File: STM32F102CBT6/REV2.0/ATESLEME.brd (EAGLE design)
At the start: 35.3 x 57.9 mm, 55 parts, among them U1 ADXL345PATRICK, U3 AMS1117-3.3, U4 STM32F102CBT6, Y2 ABM2B-8.000MHZ-10-1-U-T

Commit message: Revision V2.0.0 was released
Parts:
- removed LPS-1: LPS22, Arduino-Sensors:LPS22H
- removed LPSC1: 4.7uF, SparkFun-Capacitors:0603
- removed LPSC2: 100nF, SparkFun-Capacitors:0603
- added APGLED, MNLED: 4.7k, SparkFun-Resistors:0603-RES
- added IRC, MS5611: 100nF, SparkFun-Capacitors:0603
- added IRR: 100, SparkFun-Resistors:0603-RES
- added IRR1: 1.5k, SparkFun-Resistors:0603-RES
- added LED1: 1k, SparkFun-Resistors:0603-RES
- added LED2: RED, SparkFun-LED:LED-0603
- added RD1, RD2: Blue, SparkFun-LED:LED-0603
- added U2: MS561101BA03-50, MS5611:SON8_MS5611_TEC
- added U5: 38kHz, SparkFun-Sensors:TSOP382
- added X1: JST-XH-04-PIN-LONG-PAD, Rembrandt Electronics - JST XH Connectors v1-0:JST-XH-04-PACKAGE-LONG-PAD
- SCL_3V3, SDA_3V3: value 4.7k -> 10k
- moved RRO 2.44 mm to (7.92, 11.3)
- moved RD 2.42 mm to (7.87, 15.4)
- moved RC3 1.79 mm to (11.8, 12.7)
- moved F 1.35 mm to (10.4, 16.9), turned to 90 degrees
- moved VBAT_U 1.28 mm to (24.5, 23.4)
- moved RC4 1.12 mm to (12.1, 9.35)
- moved S 0.77 mm to (21.5, 49.0)
- moved ESDA 0.68 mm to (32.4, 45.4)
- moved ADXLC 0.68 mm to (7.34, 42.6)
- moved APGRU 0.68 mm to (31.9, 35.7)
- moved ESDM 0.68 mm to (11.3, 50.2)
- moved OSCC1 0.68 mm to (10.4, 35.3)
- moved VDD1 0.68 mm to (25.5, 36.6)
- moved VDD2 0.68 mm to (12.6, 35.8)
- moved BOOT0 0.68 mm to (17.0, 40.8)
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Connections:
- removed net INT1: LPS-1.7, U4.41
- new net IR_OUT: IRR1.1, U4.11, U5.1
- new net LED2: LED1.1, U4.15
- new net N$3: MNLED.1, RD1.A
- new net N$4: APGLED.1, RD2.A
- new net N$5: IRC.1, IRR.1, U5.3
- new net N$6: LED1.2, LED2.A
- new net RX1: U4.31, X1.2
- new net TX1: U4.30, X1.3
- net 3.3V: now also IRR.2, MS5611.1, U2.1, U2.2, X1.1; no longer LPS-1.1, LPS-1.10, LPS-1.6, LPSC1.1, LPSC2.1
- net GND: now also IRC.2, IRR1.2, LED2.C, MS5611.2, RD1.C, RD2.C, U2.3, U2.4, U2.5, U5.2, X1.4; no longer LPS-1.3, LPS-1.5, LPS-1.8, LPS-1.9, LPSC1.2, LPSC2.2
- net SCL_3V3: now also U2.8; no longer LPS-1.2
- net SDA_3V3: now also U2.7; no longer LPS-1.4
- net VAPG: now also APGLED.2
- net VMN: now also MNLED.2
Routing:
- net IR_OUT: track 0.00 -> 20.9 mm, vias 0 -> 1
- net VAPG: track 29.6 -> 49.1 mm
- net TX1: track 0.00 -> 16.6 mm, vias 0 -> 1
- net RX1: track 0.00 -> 14.8 mm, vias 0 -> 1
- net SCL_3V3: track 30.8 -> 19.1 mm
- net INT1: track 10.6 -> 0.00 mm, vias 2 -> 0
- net VMN: track 16.5 -> 22.7 mm
- net N$5: track 0.00 -> 5.12 mm
- net LED2: track 0.00 -> 3.22 mm, vias 0 -> 1
- net N$6: track 0.00 -> 2.39 mm
- net N$3: track 0.00 -> 2.22 mm
- net N$4: track 0.00 -> 2.22 mm
- net VIN: track 113.5 -> 115.7 mm
- net GND: track 1.24 -> 2.89 mm, vias 21 -> 19
- net 3.3V: track 142.0 -> 140.5 mm
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
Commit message: Version 2.0 was updated by brain.dll
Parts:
- added HOLDR, WPR: 10k, SparkFun-Resistors:0603-RES
- added IC1: WS2811-SOP8, adafruit:SO08-SKINNYPADS
- moved IRC 30.2 mm to (33.3, 26.6), flipped to the bottom, turned to 90 degrees
- moved IRR 29.1 mm to (31.0, 26.7), flipped to the bottom
- moved IRR1 28.4 mm to (32.9, 15.8), flipped to the bottom, turned to 270 degrees
- moved S2 28.1 mm to (33.3, 46.5), flipped to the bottom
- moved MNRU 28.0 mm to (33.2, 49.2), flipped to the bottom
- moved U5 27.3 mm to (32.8, 21.4), turned to 90 degrees
- moved MNRD 27.1 mm to (32.8, 40.0), flipped to the bottom
- moved ESDA 26.2 mm to (6.15, 45.9), flipped to the bottom
- moved APGRD 25.4 mm to (6.55, 32.7), flipped to the bottom
- moved APGRU 25.4 mm to (6.58, 36.2), flipped to the bottom
- moved Y2 24.2 mm to (31.3, 33.8), flipped to the bottom
- moved ADXLC 23.8 mm to (31.2, 43.1), flipped to the bottom
- moved RD 22.8 mm to (30.6, 15.8), flipped to the bottom
- moved RRO 22.7 mm to (30.6, 11.8), flipped to the bottom
- moved X1 21.1 mm to (8.71, 22.2), flipped to the top
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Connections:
- removed net PC13: U4.2
- new net CS: IC1.1, U4.25
- new net HOLD: HOLDR.1, IC1.7, U4.29
- new net MISO: IC1.2, U4.27
- new net MOSI: IC1.5, U4.28
- new net SCK: IC1.6, U4.26
- new net WP: IC1.3, U4.2, WPR.2
- net 3.3V: now also HOLDR.2, IC1.8
- net GND: now also IC1.4, WPR.1
- net LED2: now also U4.40; no longer U4.15
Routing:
- net 3.3V: track 140.5 -> 154.3 mm, vias 6 -> 7
- net CS: track 0.00 -> 10.8 mm, vias 0 -> 1
- net HOLD: track 0.00 -> 9.58 mm, vias 0 -> 1
- net MISO: track 0.00 -> 8.24 mm, vias 0 -> 1
- net WP: track 0.00 -> 7.57 mm, vias 0 -> 1
- net MOSI: track 0.00 -> 5.01 mm, vias 0 -> 1
- net SCK: track 0.00 -> 4.83 mm, vias 0 -> 1
- net GND: track 2.89 -> 0.00 mm, vias 19 -> 21
- net SDA_3V3: track 16.9 -> 14.5 mm
- net SCL_3V3: track 19.1 -> 18.4 mm, vias 0 -> 2
- added copper zone on layer 16, net HT
- removed copper zone on layer 1, net HT
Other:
- outline, holes or cut-outs redrawn

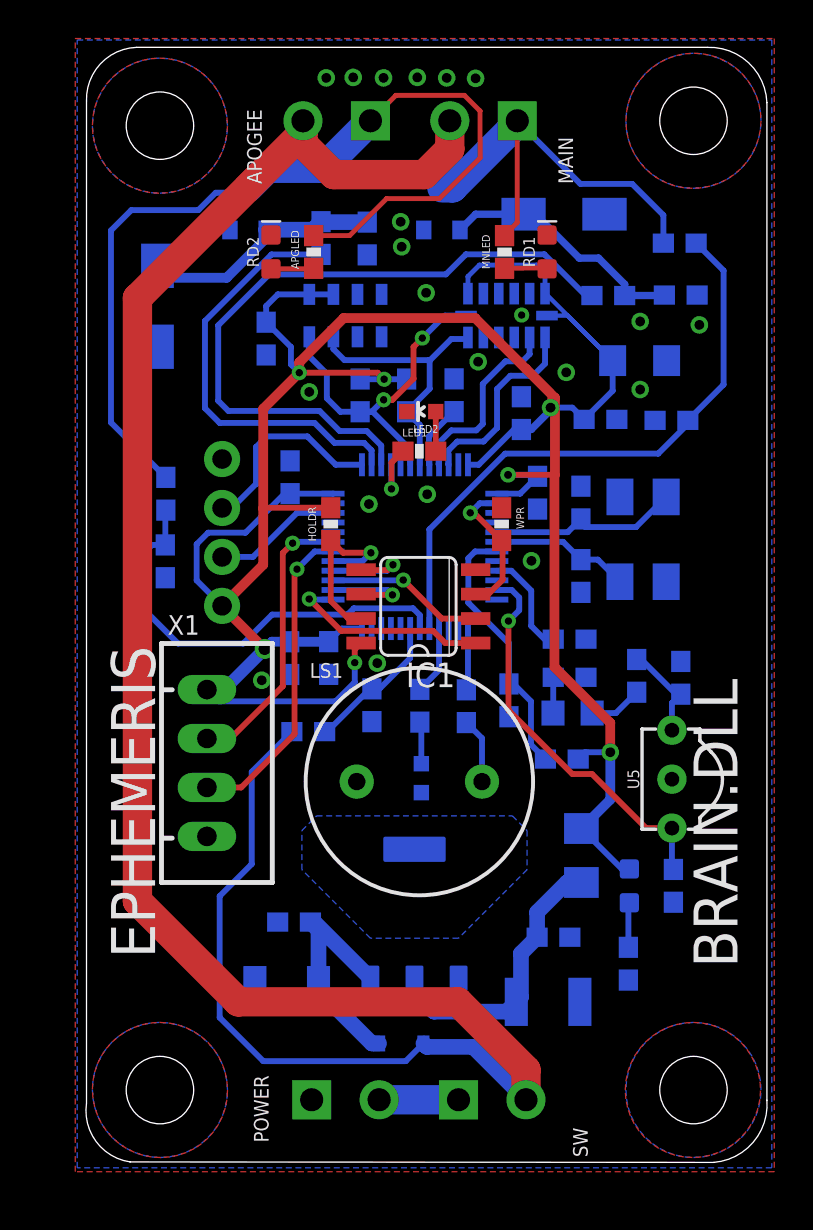
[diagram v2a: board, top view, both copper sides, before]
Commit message: VDDA cap calue was changed
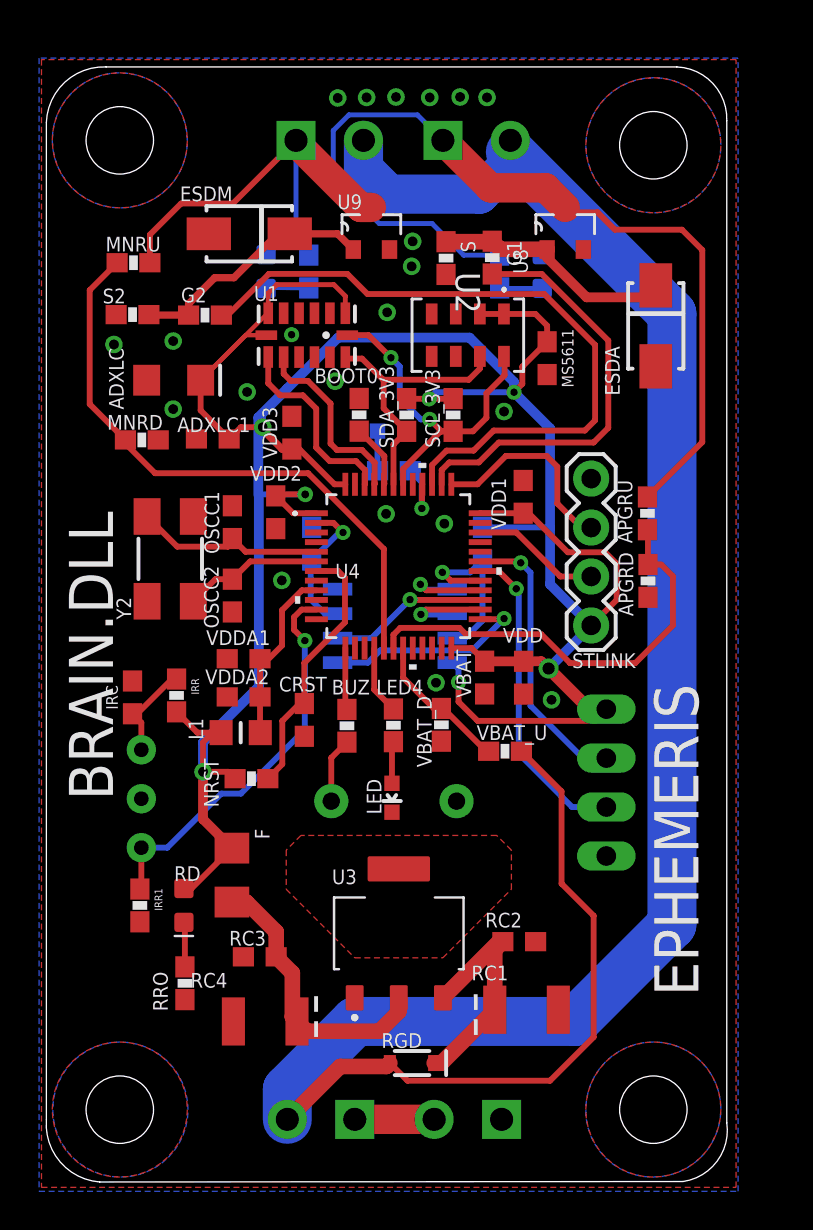
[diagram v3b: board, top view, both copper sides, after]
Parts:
- IC1: value WS2811-SOP8 -> EN25F40-100GCP-TR
- S, S2: value 3.3k -> 4.7k
- U8, U9: value (none) -> SI2308CDS-T1-GE3
- VDDA2: value 100nF -> 10nF
- moved IRC 28.5 mm to (4.85, 25.6), flipped to the top
- moved S2 28.5 mm to (4.85, 45.5), flipped to the top
- moved MNRU 28.4 mm to (4.90, 48.2), flipped to the top
- moved IRR1 27.7 mm to (5.23, 14.8), flipped to the top
- moved U5 27.6 mm to (5.31, 20.4), flipped to the bottom
- moved MNRD 27.5 mm to (5.33, 39.0), flipped to the top
- moved ESDA 25.9 mm to (32.0, 44.9), flipped to the top
- moved APGRD 25.1 mm to (31.6, 31.7), flipped to the top
- moved APGRU 25.0 mm to (31.6, 35.2), flipped to the top
- moved Y2 24.6 mm to (6.81, 32.8), flipped to the top
- moved ADXLC 24.2 mm to (6.99, 42.1), flipped to the top
- moved IRR 23.9 mm to (7.14, 25.7), flipped to the top
- moved RD 23.1 mm to (7.52, 14.8), flipped to the top
- moved RRO 23.0 mm to (7.57, 10.8), flipped to the top
- moved G2 21.0 mm to (8.61, 45.5), flipped to the top
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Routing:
- added copper zone on layer 1, net HT
- removed copper zone on layer 16, net HT
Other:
- outline, holes or cut-outs redrawn
